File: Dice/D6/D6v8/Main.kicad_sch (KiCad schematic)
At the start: 31 parts, among them J1 Conn_01x14, J2 Conn_01x04, J4 DNP, U1 N52810_QFN32, U2 KXTJ3-1057, Y1 32MHz 40ppm

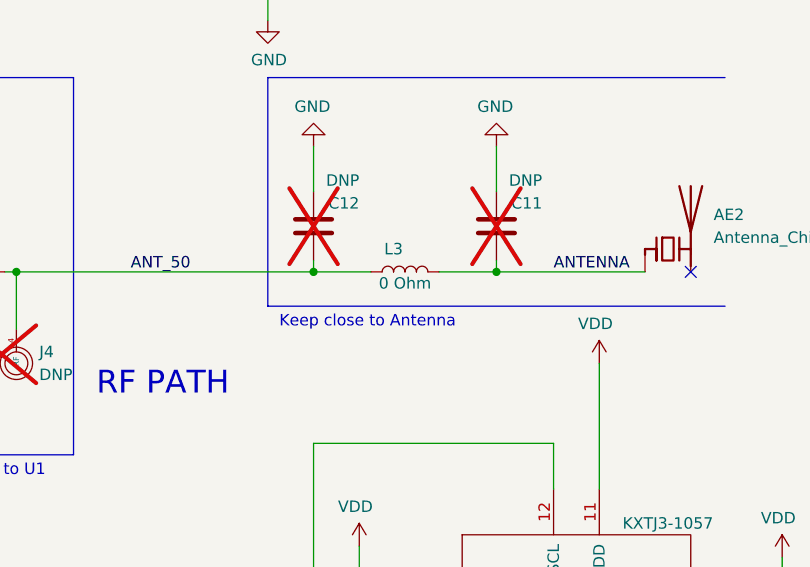
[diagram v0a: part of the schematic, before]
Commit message: Updated LCC PCB, updated dice fpc. Moved LCC testing jig
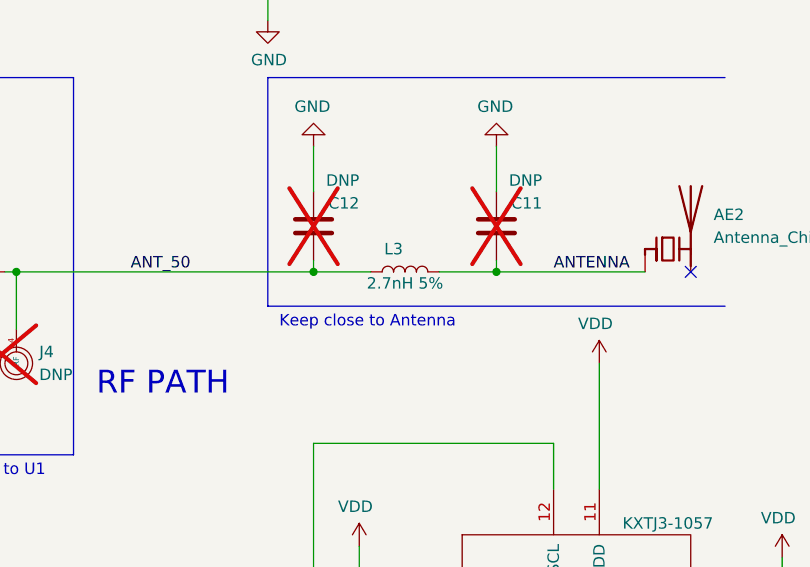
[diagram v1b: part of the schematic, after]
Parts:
- L3: value 0 Ohm -> 2.7nH 5%; Manufacturer UNI-ROYAL(Uniroyal Elec) -> Murata; Manufacturer Part Number 0402WGJ0000TCE -> LQG15HN2N7C02D
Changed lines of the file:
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@@
       (effects (font (size 1.27 1.27)))
     )
-    (property "Value" "0 Ohm" (at 237.49 97.79 90)
+    (property "Value" "2.7nH 5%" (at 237.49 97.79 90)
       (effects (font (size 1.27 1.27)))
     )
@@
       (effects (font (size 1.27 1.27)) hide)
     )
-    (property "Manufacturer" "UNI-ROYAL(Uniroyal Elec)" (at 237.49 96.52 0)
+    (property "Manufacturer" "Murata" (at 237.49 96.52 0)
       (effects (font (size 1.27 1.27)) hide)
     )
-    (property "Manufacturer Part Number" "0402WGJ0000TCE" (at 237.49 96.52 0)
+    (property "Manufacturer Part Number" "LQG15HN2N7C02D" (at 237.49 96.52 0)
       (effects (font (size 1.27 1.27)) hide)
     )
